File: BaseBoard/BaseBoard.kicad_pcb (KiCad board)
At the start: 2 copper layers, 55 x 55 mm, 64 parts, among them J2 54-00167, SW1 SW_Push, SW2 SW_Push, U1 TPS548A28, U10 USB Type C, U11 PRTR5V0U2X, U2 TPS54202DDC, U3 SN74AVC4T774, U4 RT9078N-08GJ5, U5 EMC2101, U6 ESP32-S3-MINI-1, Y1 32.768kHz

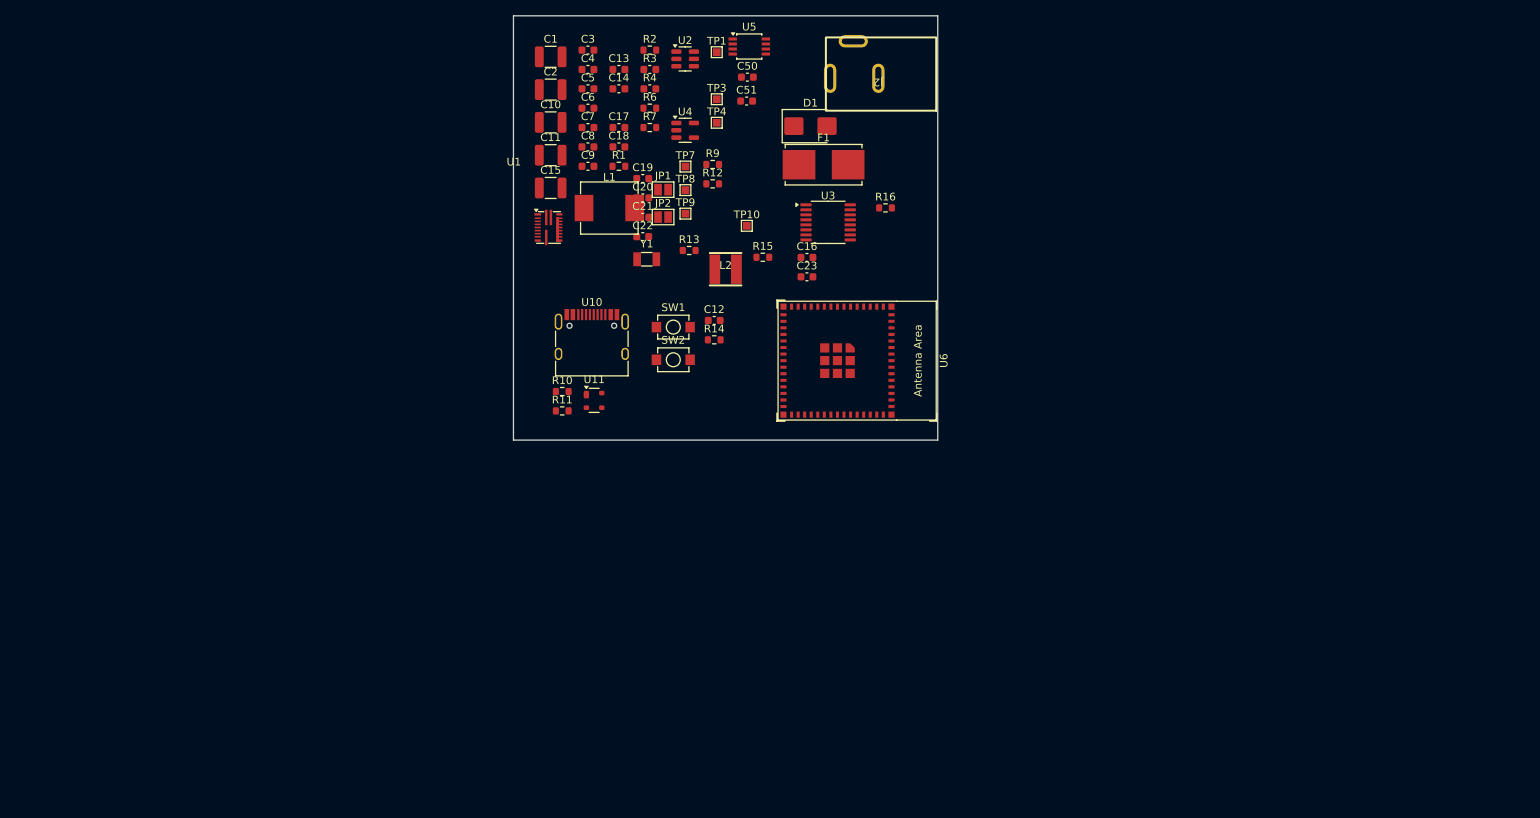
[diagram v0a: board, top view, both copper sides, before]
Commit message: Added support for TMP1075 temperature sensor to monitor ASIC
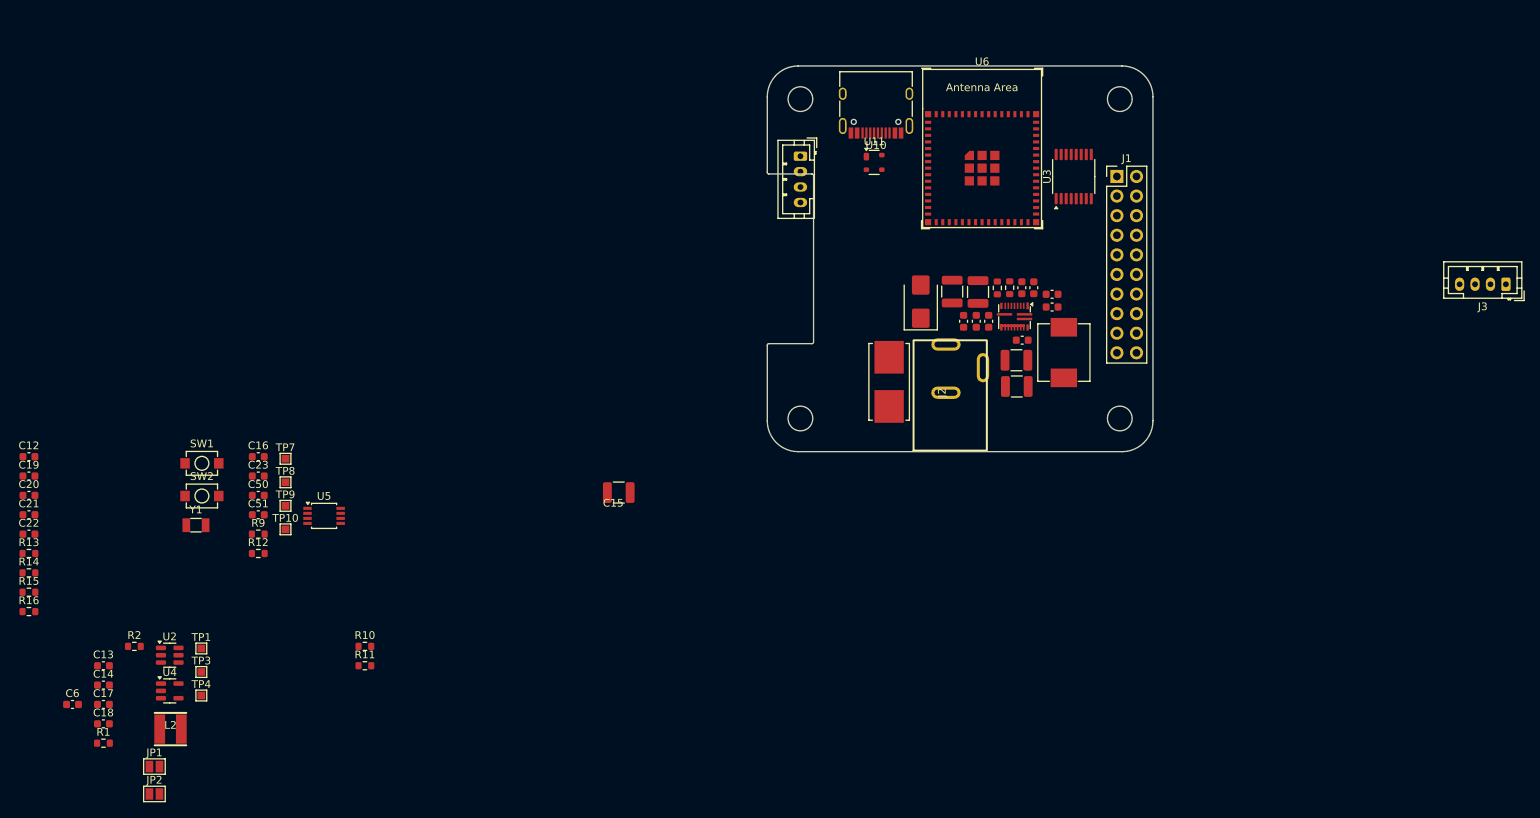
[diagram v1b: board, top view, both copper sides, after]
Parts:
- added H1: MountingHole, MountingHole:MountingHole_3.2mm_M3, F.Cu at (128.3, 72.3)
- added H2: MountingHole, MountingHole:MountingHole_3.2mm_M3, F.Cu at (169.7, 72.3)
- added H3: MountingHole, MountingHole:MountingHole_3.2mm_M3, F.Cu at (169.7, 113.7)
- added H4: MountingHole, MountingHole:MountingHole_3.2mm_M3, F.Cu at (128.3, 113.7)
- added J1: Conn_02x10_Odd_Even, Connector_PinHeader_2.54mm:PinHeader_2x10_P2.54mm_Vertical, F.Cu at (169.3, 82.3)
- added J3: SSD1306 OLED Display, Connector_JST:JST_PH_B4B-PH-K_1x04_P2.00mm_Vertical, F.Cu at (219.8, 96.3)
- added J4: FAN, Connector_JST:JST_PH_B4B-PH-K_1x04_P2.00mm_Vertical, F.Cu at (128.3, 79.7)
- moved R16 122.7 mm to (28.3, 138.7)
- moved R15 104.6 mm to (28.3, 136.2)
- moved C6 102.2 mm to (33.9, 150.8)
- moved R2 102.2 mm to (42.0, 143.2)
- moved C13 102.2 mm to (38.0, 145.8)
- moved C14 102.2 mm to (38.0, 148.3)
- moved TP1 102.2 mm to (50.6, 143.5)
- moved U2 102.2 mm to (46.5, 144.4)
- moved C17 100.3 mm to (38.0, 150.8)
- moved C18 100.3 mm to (38.0, 153.3)
- moved R1 100.3 mm to (38.0, 155.8)
- moved TP4 99.9 mm to (50.6, 149.6)
- moved TP3 99.9 mm to (50.6, 146.6)
- moved JP1 99.7 mm to (44.6, 158.8)
- moved JP2 99.7 mm to (44.6, 162.4)
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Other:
- board size 55 x 55 mm -> 50 x 50 mm
- copper layers 2 -> 4
